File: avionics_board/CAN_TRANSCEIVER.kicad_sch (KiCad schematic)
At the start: 8 parts, among them U7 TCAN3414

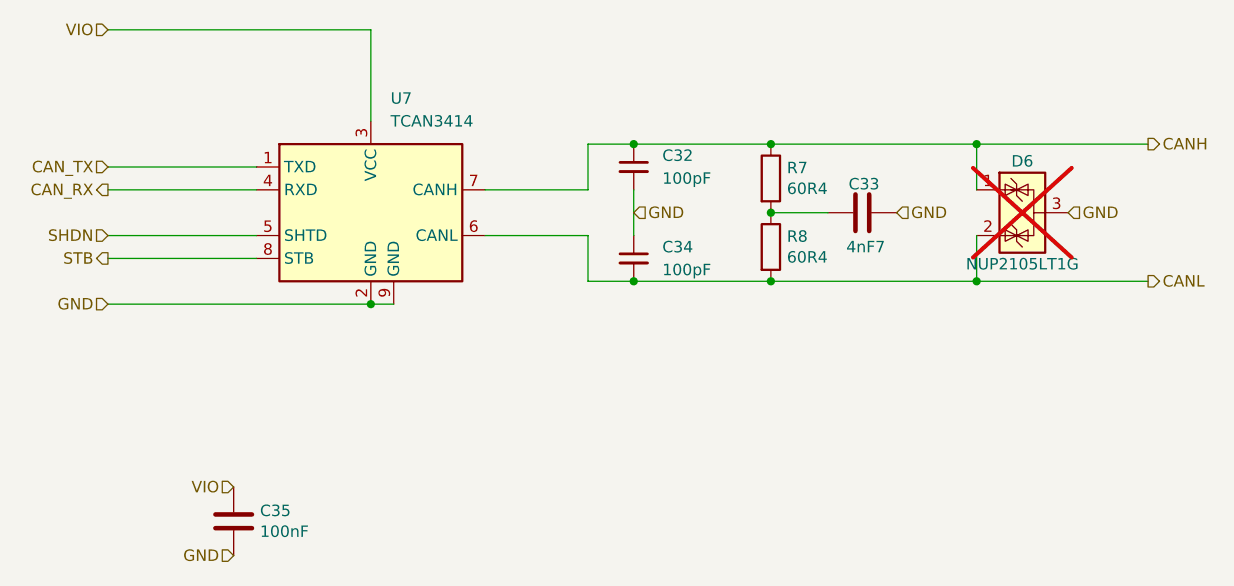
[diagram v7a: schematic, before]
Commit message: move project to new location, update sympbol, footprint and step paths
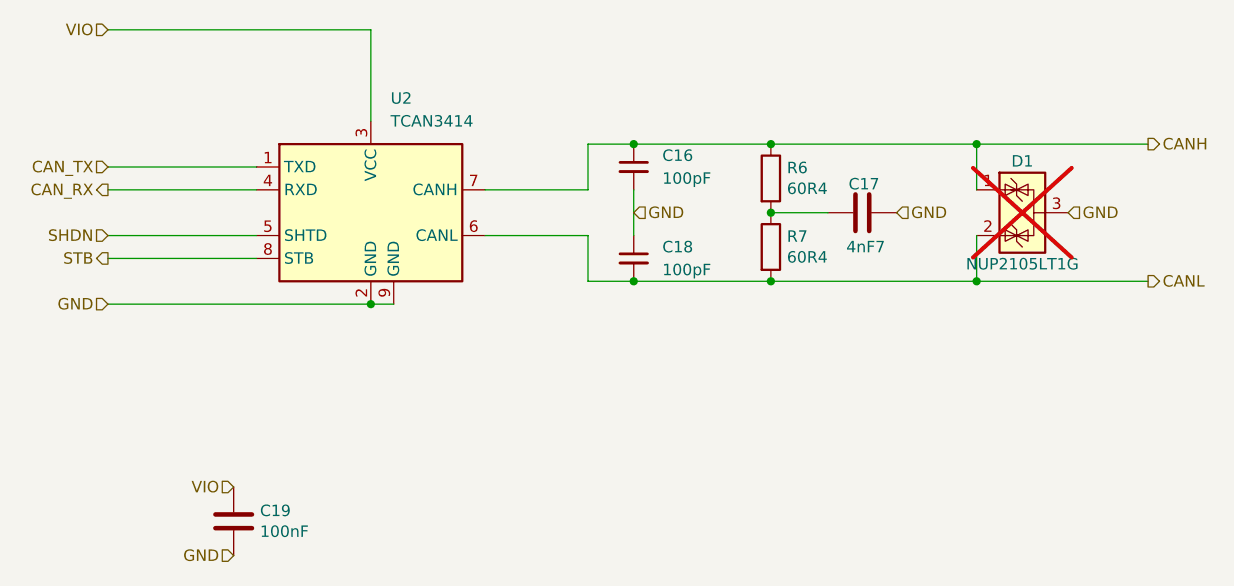
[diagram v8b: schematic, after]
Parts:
- renumbered C32 to C16, C33 to C17, C34 to C18, C35 to C19, D6 to D1, R7 to R6, R8 to R7, U7 to U2
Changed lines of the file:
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@@
 		(on_board yes)
 		(dnp no)
-		(property "Reference" "R7"
+		(property "Reference" "R6"
 			(at 166.878 86.4616 0)
 			(effects
@@
 			(project "sci_board"
 				(path "/b4b2c88d-f6cd-4e60-862d-e21f68728580/1a2691c5-5723-4a0d-b1a6-0fb5069c9e03"
-					(reference "R12")
+					(reference "R8")
 					(unit 1)
 				)
 				(path "/b4b2c88d-f6cd-4e60-862d-e21f68728580/5e856d8a-328e-413a-92b7-9cd181b0cc6b"
-					(reference "R10")
+					(reference "R6")
 					(unit 1)
 				)
@@
 		(on_board yes)
 		(dnp no)
-		(property "Reference" "R8"
+		(property "Reference" "R7"
 			(at 166.878 94.0816 0)
 			(effects
@@
 			(project "sci_board"
 				(path "/b4b2c88d-f6cd-4e60-862d-e21f68728580/1a2691c5-5723-4a0d-b1a6-0fb5069c9e03"
-					(reference "R13")
+					(reference "R9")
 					(unit 1)
 				)
 				(path "/b4b2c88d-f6cd-4e60-862d-e21f68728580/5e856d8a-328e-413a-92b7-9cd181b0cc6b"
-					(reference "R11")
+					(reference "R7")
 					(unit 1)
 				)
@@
 		(on_board yes)
 		(dnp yes)
-		(property "Reference" "D6"
+		(property "Reference" "D1"
 			(at 193.04 85.725 90)
 			(effects
@@
 		(on_board yes)
 		(dnp no)
-		(property "Reference" "C33"
+		(property "Reference" "C17"
 			(at 177.165 88.265 90)
 			(effects
@@
 		(on_board yes)
 		(dnp no)
-		(property "Reference" "C35"
+		(property "Reference" "C19"
 			(at 108.331 124.5616 0)
 			(effects
@@
 		(dnp no)
 		(fields_autoplaced yes)
-		(property "Reference" "C32"
+		(property "Reference" "C16"
 			(at 153.035 85.0962 0)
 			(effects
@@
 		(dnp no)
 		(fields_autoplaced yes)
-		(property "Reference" "C34"
+		(property "Reference" "C18"
 			(at 153.035 95.2562 0)
 			(effects
@@
 		(dnp no)
 		(fields_autoplaced yes)
-		(property "Reference" "U7"
+		(property "Reference" "U2"
 			(at 122.8441 78.74 0)
 			(effects
